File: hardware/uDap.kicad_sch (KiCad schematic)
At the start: 6 parts, among them J1 USB_C_Receptacle_USB2.0_16P, J2 Conn_02x04_Odd_Even, U1 CH32X035F8U6, U2 RT9013

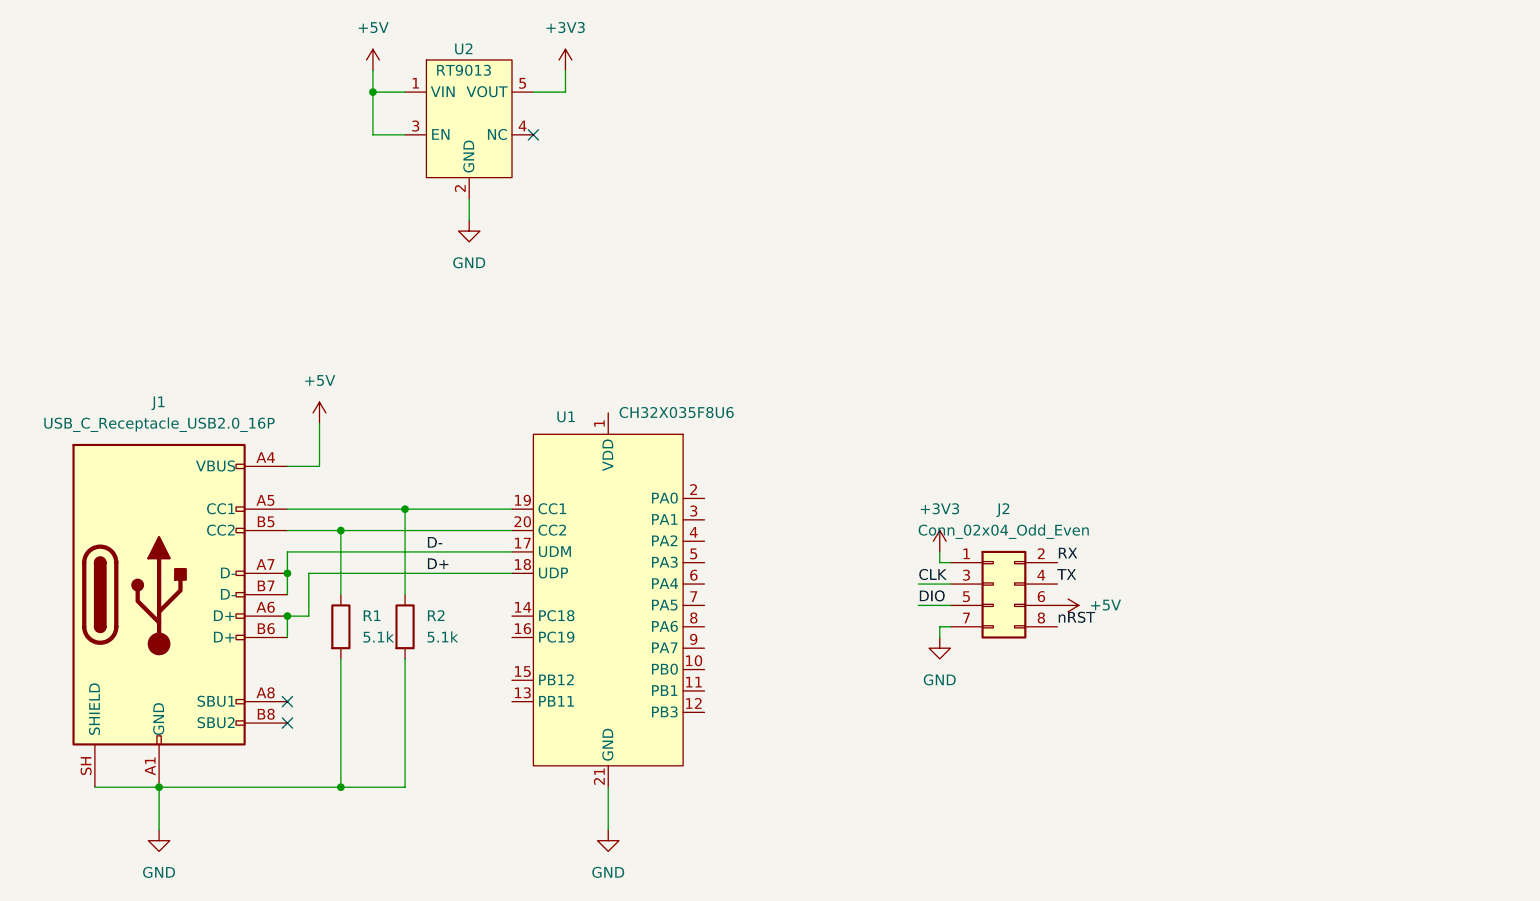
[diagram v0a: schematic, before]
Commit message: 完善了 udap-ch32x035 整体的功能
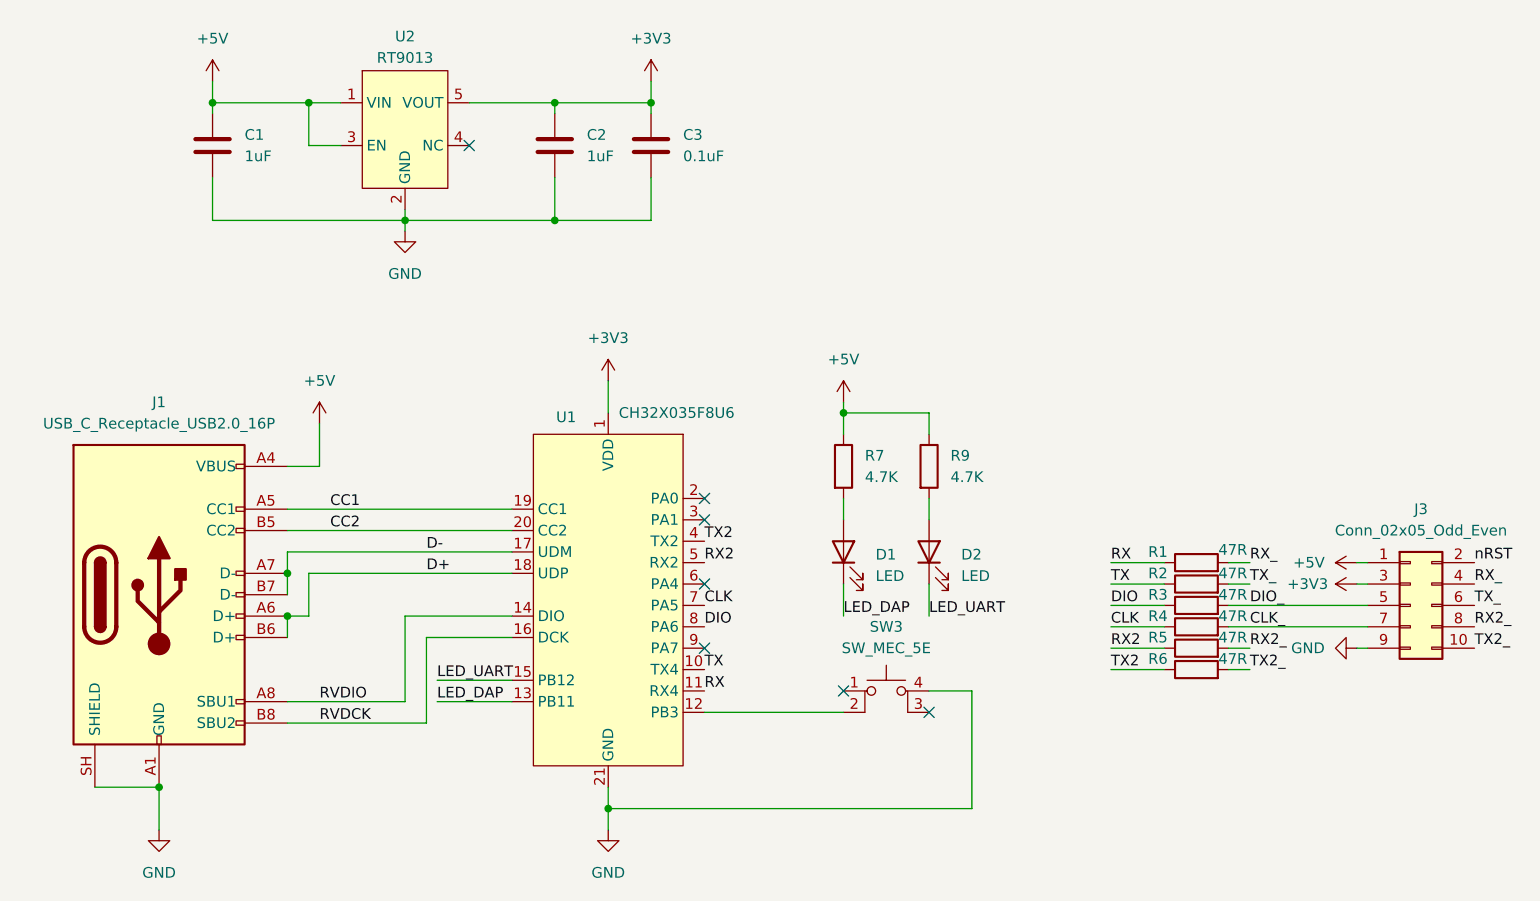
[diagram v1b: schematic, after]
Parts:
- removed J2: Conn_02x04_Odd_Even, Connector_PinHeader_2.54mm:PinHeader_2x04_P2.54mm_Vertical, symbol Connector_Generic:Conn_02x04_Odd_Even
- added C1, C2: 1uF, Capacitor_SMD:C_0603_1608Metric, symbol Device:C
- added C3: 0.1uF, Capacitor_SMD:C_0603_1608Metric, symbol Device:C
- added D1, D2: LED, LED_SMD:LED_0603_1608Metric, symbol Device:LED
- added J3: Conn_02x05_Odd_Even, my_connector:双面贴片排针2x5, symbol Connector_Generic:Conn_02x05_Odd_Even
- added R3, R4, R5, R6: 47R, Resistor_SMD:R_0603_1608Metric, symbol Device:R
- added R7, R9: 4.7K, Resistor_SMD:R_0603_1608Metric, symbol Device:R
- added SW3: SW_MEC_5E, my_footprint:KEY-SMD_4P-L4.2-W3.4-P2.15-LS4.5-TL_1, symbol Switch:SW_MEC_5E
- R1, R2: value 5.1k -> 47R; footprint Resistor_SMD:R_0402_1005Metric -> Resistor_SMD:R_0603_1608Metric
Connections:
- net +3V3: now also U1.1 (VDD), C2.1, C3.1, J3.3 (Pin_3)
- net +5V: now also C1.1, J3.1 (Pin_1), R7.1, R9.1
- net CLK: now also U1.7 (PA5), R4.1
- net DIO: now also U1.8 (PA6), R3.1
- net GND: now also C1.2, C2.2, C3.2, J3.9 (Pin_9), SW3.4 (A); no longer R1.2, R2.2
- net RX: now also R1.1, U1.11 (PB1)
- net TX: now also R2.1, U1.10 (PB0)
- net nRST: now also J3.2 (Pin_2)
- net CC2: now reaches J1.B5 (CC2), U1.20 (PC15)
- net CC2: no longer R1.1
- net CC1: now reaches J1.A5 (CC1), U1.19 (PC14)
- net CC1: no longer R2.1
- net RVDIO: now reaches J1.A8 (SBU1)
- net RVDIO: now also U1.14 (PC18)
- net RVDCK: now reaches J1.B8 (SBU2)
- net RVDCK: now also U1.16 (PC19)
- net at U1.12 (PB3): now also SW3.2
- net LED_DAP: now reaches U1.13 (PB11)
- net LED_DAP: now also D1.1 (K)
- net LED_UART: now reaches U1.15 (PB12)
- net LED_UART: now also D2.1 (K)
- net TX2: now reaches U1.4 (PA2)
- net TX2: now also R6.1
- net RX2: now reaches U1.5 (PA3)
- net RX2: now also R5.1
- new net: D1.2 (A), R7.2
- new net: D2.2 (A), R9.2
- new net CLK_: J3.7 (Pin_7), R4.2
- new net DIO_: J3.5 (Pin_5), R3.2
- new net RX2_: J3.8 (Pin_8), R5.2
- new net RX_: J3.4 (Pin_4), R1.2
- new net TX2_: J3.10 (Pin_10), R6.2
- new net TX_: J3.6 (Pin_6), R2.2
- no-connect marks 3 -> 7
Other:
- title: (none) -> ch32x035-uDap
- moved on the sheet: U2
